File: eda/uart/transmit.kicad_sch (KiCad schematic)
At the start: 7 parts, among them U1 74HCT193, U16 74HCT74, U2 74HCT165, U3 74HCT165

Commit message: Uart and loader work
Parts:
- renumbered C4 to C7, C4 to C8, C4 to C9, U1 to U4, U3 to U5, U2 to U6
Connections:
- net FIFO Transmit/DOR: now also U16.2 (D); no longer U16.12 (D)
- net UartClock: now also U16.3 (C); no longer U16.11 (C)
- net VCC: now also U16.4 (~{S}); no longer U16.10 (~{S})
- net ~{ClockEnable}: now also U16.6 (~{Q}); no longer U16.8 (~{Q})
- net ~{LatchShiftRegisters}: now also U16.5 (Q); no longer U16.9 (Q)
- net at U4.13 (~{BO}): now also U16.1 (~{R}); no longer U16.13 (~{R})

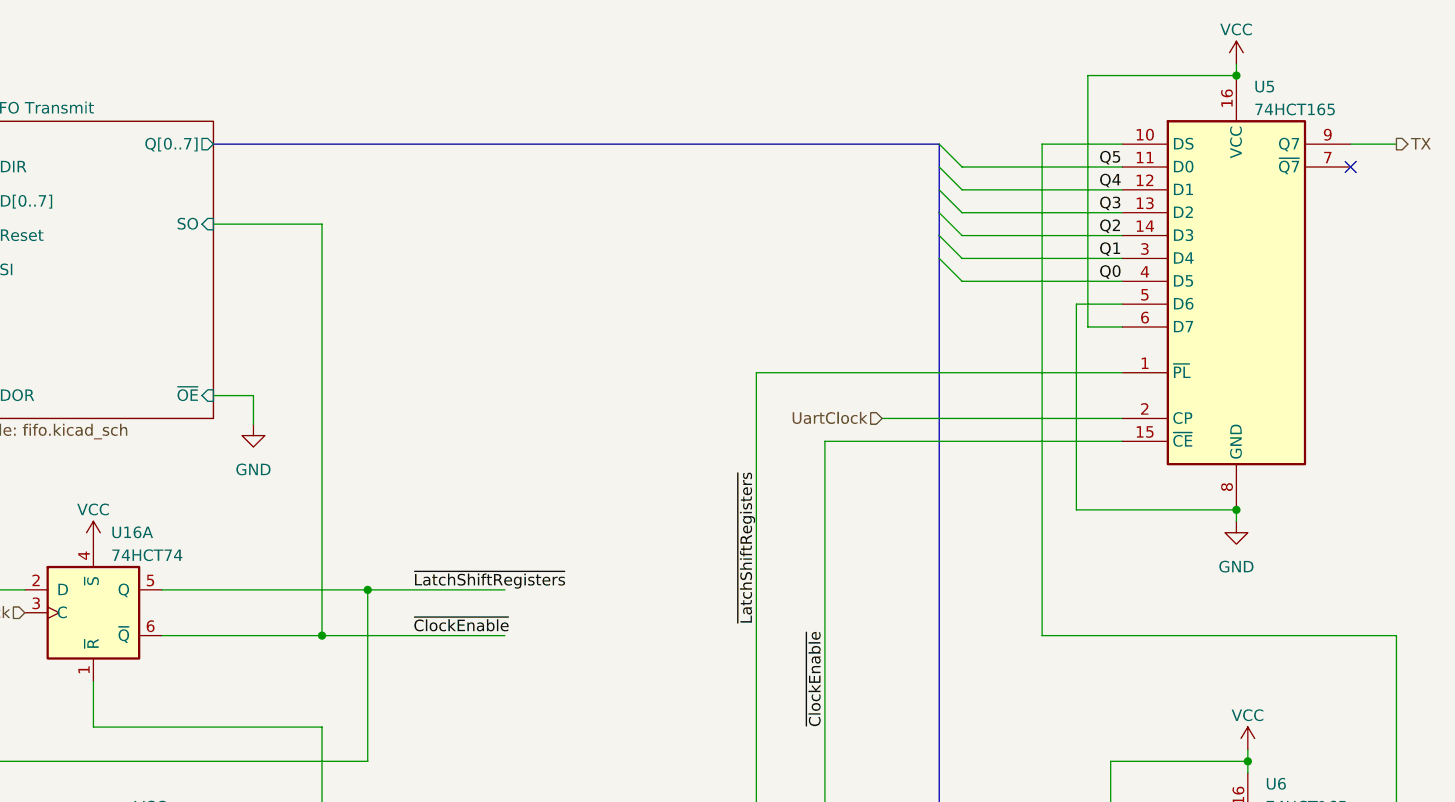
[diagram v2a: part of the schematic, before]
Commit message: Uart board to v1.1...make bodges permanent :(
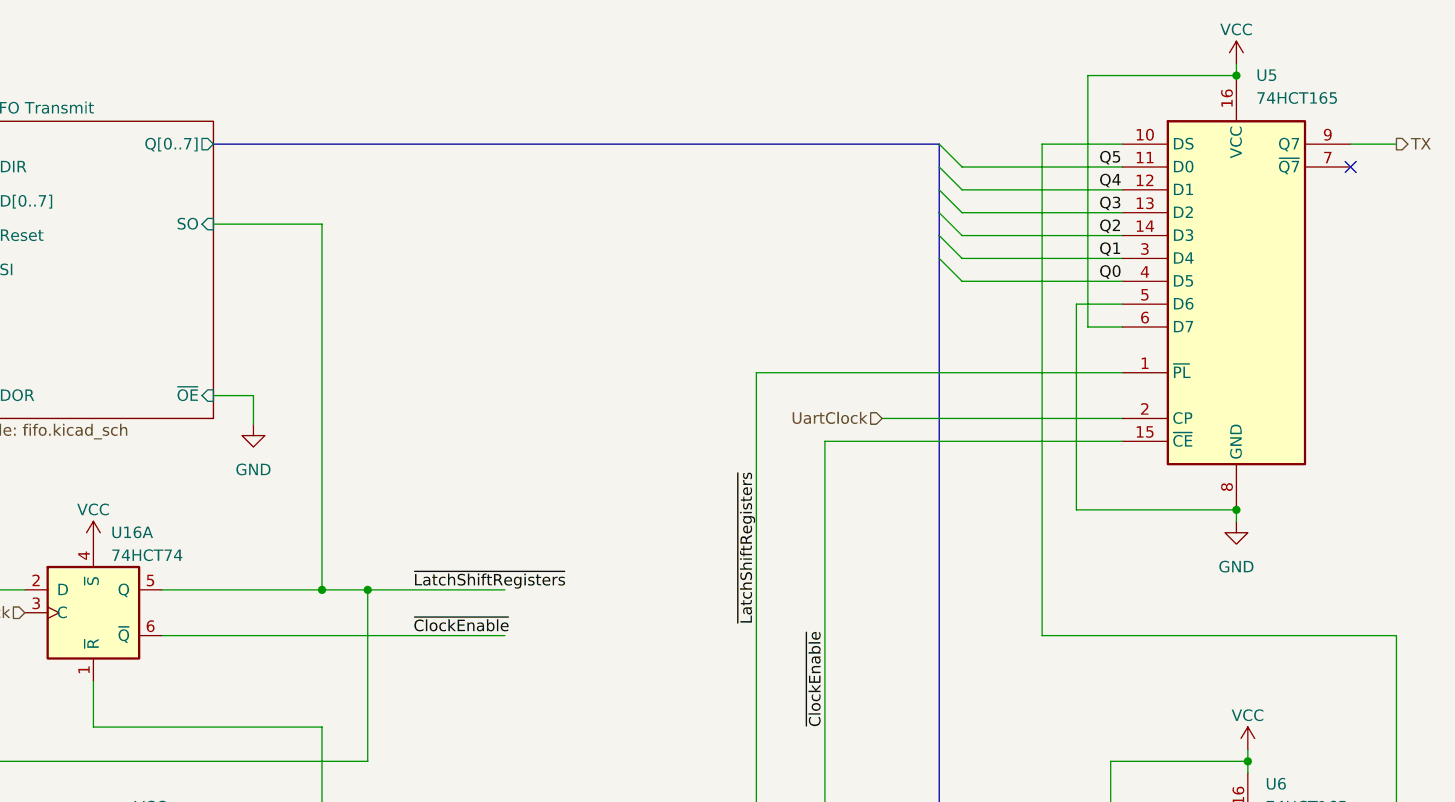
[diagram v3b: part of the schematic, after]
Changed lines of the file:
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@@
+	)
+	(junction
+		(at 198.12 113.03)
+		(diameter 0)
+		(color 0 0 0 0)
 	)
 	(junction
@@
 	)
 	(junction
-		(at 198.12 113.03)
+		(at 35.56 185.42)
+		(diameter 0)
+		(color 0 0 0 0)
+	)
+	(junction
+		(at 72.39 144.78)
+		(diameter 0)
+		(color 0 0 0 0)
+	)
+	(junction
+		(at 91.44 114.3)
 		(diameter 0)
 		(color 0 0 0 0)
@@
 	)
 	(junction
-		(at 35.56 185.42)
-		(diameter 0)
-		(color 0 0 0 0)
-	)
-	(junction
-		(at 72.39 144.78)
-		(diameter 0)
-		(color 0 0 0 0)
-	)
-	(junction
-		(at 91.44 114.3)
-		(diameter 0)
-		(color 0 0 0 0)
-	)
-	(junction
 		(at 213.36 101.6)
 		(diameter 0)
@@
 	)
 	(junction
-		(at 110.49 87.63)
+		(at 74.93 127)
 		(diameter 0)
 		(color 0 0 0 0)
 	)
 	(junction
-		(at 74.93 127)
+		(at 110.49 82.55)
 		(diameter 0)
 		(color 0 0 0 0)
@@
 	(wire
 		(pts
-			(xy 110.49 87.63) (xy 92.71 87.63)
-		)
-		(stroke
-			(width 0)
-			(type default)
-		)
-	)
-	(wire
-		(pts
 			(xy 198.12 125.73) (xy 200.66 125.73)
 		)
@@
 	(wire
 		(pts
-			(xy 110.49 87.63) (xy 130.81 87.63)
+			(xy 92.71 87.63) (xy 130.81 87.63)
 		)
 		(stroke
@@
 	(wire
 		(pts
+			(xy 110.49 82.55) (xy 115.57 82.55)
+		)
+		(stroke
+			(width 0)
+			(type default)
+		)
+	)
+	(wire
+		(pts
 			(xy 158.75 58.42) (xy 199.39 58.42)
 		)
@@
 	(wire
 		(pts
+			(xy 110.49 41.91) (xy 110.49 82.55)
+		)
+		(stroke
+			(width 0)
+			(type default)
+		)
+	)
+	(wire
+		(pts
 			(xy 72.39 121.92) (xy 78.74 121.92)
 		)
@@
 		)
 	)
-	(wire
-		(pts
-			(xy 110.49 41.91) (xy 110.49 87.63)
-		)
-		(stroke
-			(width 0)
-			(type default)
-		)
-	)
 	(bus
 		(pts
@@
 	(wire
 		(pts
-			(xy 92.71 82.55) (xy 115.57 82.55)
+			(xy 92.71 82.55) (xy 110.49 82.55)
 		)
 		(stroke
@@
 	)
 	(symbol
+		(lib_id "74xx:74LS165")
+		(at 212.09 48.26 0)
+		(unit 1)
+		(exclude_from_sim no)
+		(in_bom yes)
+		(on_board yes)
+		(dnp no)
+		(fields_autoplaced yes)
+		(property "Reference" "U5"
+			(at 214.2841 25.4 0)
+			(effects
+				(font
+					(size 1.27 1.27)
+				)
+				(justify left)
+			)
+		)
+		(property "Value" "74HCT165"
+			(at 214.2841 27.94 0)
+			(effects
+				(font
+					(size 1.27 1.27)
+				)
+				(justify left)
+			)
+		)
+		(property "Footprint" "Package_DIP:DIP-16_W7.62mm"
+			(at 212.09 48.26 0)
+			(effects
+				(font
+					(size 1.27 1.27)
+				)
+				(hide yes)
+			)
+		)
+		(property "Datasheet" "https://www.ti.com/lit/ds/symlink/sn74ls165a.pdf"
+			(at 212.09 48.26 0)
+			(effects
+				(font
+					(size 1.27 1.27)
+				)
+				(hide yes)
+			)
+		)
+		(property "Description" ""
+			(at 212.09 48.26 0)
+			(effects
+				(font
+					(size 1.27 1.27)
+				)
+				(hide yes)
+			)
+		)
+		(pin "1"
+		)
+		(pin "10"
+		)
+		(pin "11"
+		)
+		(pin "12"
+		)
+		(pin "13"
+		)
+		(pin "14"
+		)
+		(pin "15"
+		)
+		(pin "16"
+		)
+		(pin "2"
+		)
+		(pin "3"
+		)
+		(pin "4"
+		)
+		(pin "5"
+		)
+		(pin "6"
+		)
+		(pin "7"
+		)
+		(pin "8"
+		)
+		(pin "9"
+		)
+		(instances
+			(project "uart"
+				(path "/11545594-d6d6-4b37-a578-fa23933d5773/58e4c198-6a2b-4c28-a1a8-589b85574c34"
+					(reference "U5")
+					(unit 1)
+				)
+			)
+		)
+	)
+	(symbol
 		(lib_id "power:VCC")
 		(at 212.09 24.13 0)
@@
 					(unit 1)
 				)
-			)
-		)
-	)
-	(symbol
-		(lib_id "74xx:74LS165")
-		(at 212.09 48.26 0)
-		(unit 1)
-		(exclude_from_sim no)
-		(in_bom yes)
-		(on_board yes)
-		(dnp no)
-		(fields_autoplaced yes)
-		(property "Reference" "U5"
-			(at 214.0459 26.67 0)
-			(effects
-				(font
-					(size 1.27 1.27)
-				)
-				(justify left)
-			)
-		)
-		(property "Value" "74HCT165"
-			(at 214.0459 29.21 0)
-			(effects
-				(font
-					(size 1.27 1.27)
-				)
-				(justify left)
-			)
-		)
-		(property "Footprint" "Package_DIP:DIP-16_W7.62mm"
-			(at 212.09 48.26 0)
-			(effects
-				(font
-					(size 1.27 1.27)
-				)
-				(hide yes)
-			)
-		)
-		(property "Datasheet" "https://www.ti.com/lit/ds/symlink/sn74ls165a.pdf"
-			(at 212.09 48.26 0)
-			(effects
-				(font
-					(size 1.27 1.27)
-				)
-				(hide yes)
-			)
-		)
-		(property "Description" ""
-			(at 212.09 48.26 0)
-			(effects
-				(font
-					(size 1.27 1.27)
-				)
-				(hide yes)
-			)
-		)
-		(pin "1"
-		)
-		(pin "10"
-		)
-		(pin "11"
-		)
-		(pin "12"
-		)
-		(pin "13"
-		)
-		(pin "14"
-		)
-		(pin "15"
-		)
-		(pin "16"
-		)
-		(pin "2"
-		)
-		(pin "3"
-		)
-		(pin "4"
-		)
-		(pin "5"
-		)
-		(pin "6"
-		)
-		(pin "7"
-		)
-		(pin "8"
-		)
-		(pin "9"
-		)
-		(instances
-			(project "uart"
-				(path "/11545594-d6d6-4b37-a578-fa23933d5773/58e4c198-6a2b-4c28-a1a8-589b85574c34"
-					(reference "U5")
-					(unit 1)
-				)
